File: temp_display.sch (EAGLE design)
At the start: 65 parts, among them IC2 ATMEGA168PROUND, Q1 2N2907

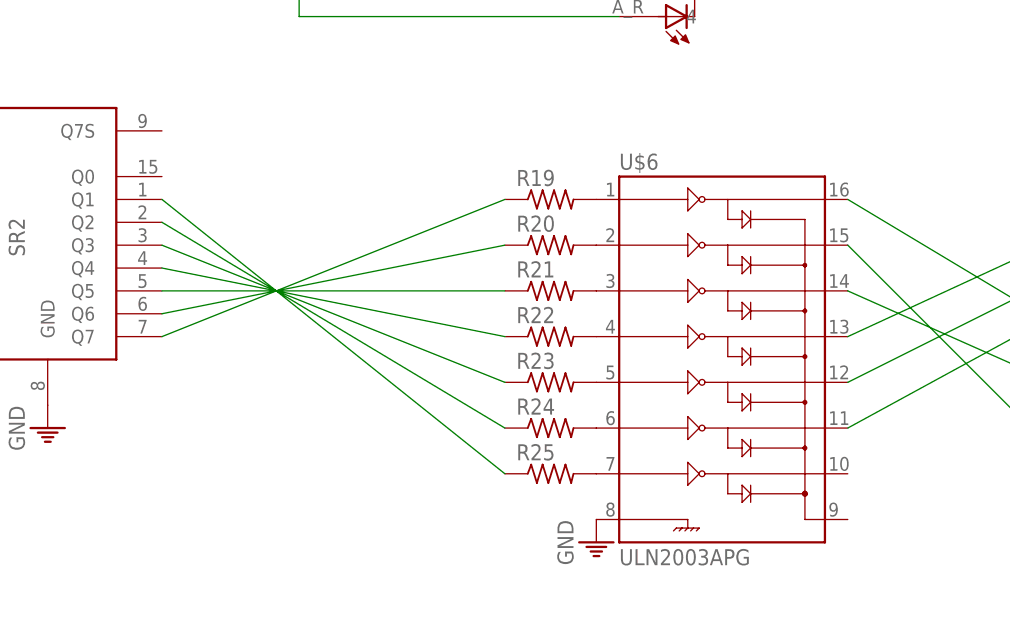
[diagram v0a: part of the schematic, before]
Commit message: Removed resistors from ULN2003 darlington array
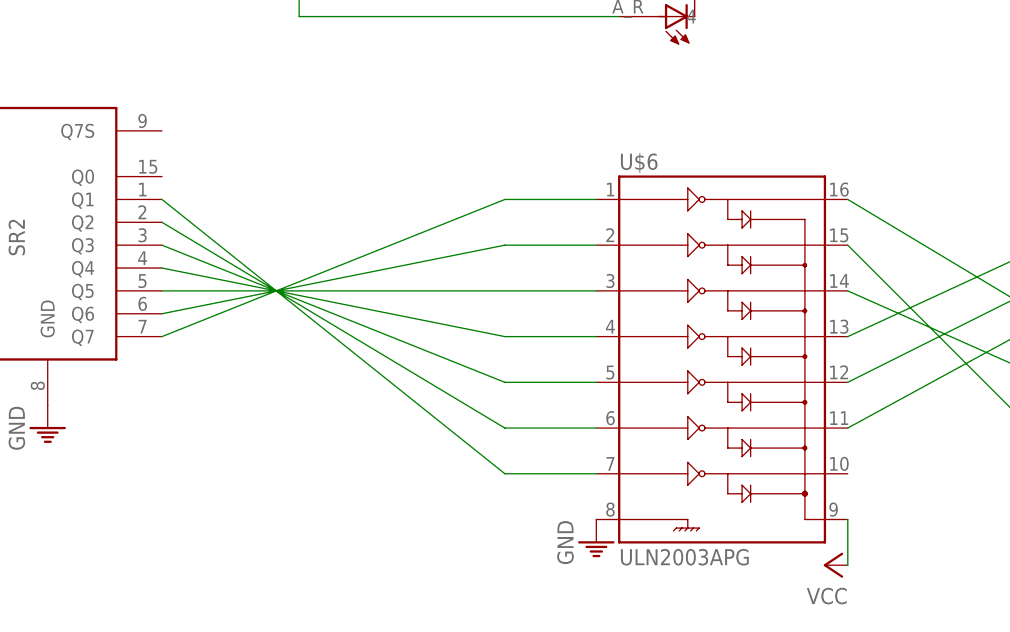
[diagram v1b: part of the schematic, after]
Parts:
- removed R19, R20, R21, R22, R23, R24, R25: (no value), resistor:R-US_0204/7
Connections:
- net N$10 renamed K_L7S_2
- net N$11 renamed K_L7S_1
- net N$13 renamed K_IL34
- net N$14 renamed K_IL12
- net N$59 renamed K_IL56
- net N$60 renamed STCP2
- net N$9 renamed K_L7S_3
- removed net N$16: R19.2, U$6.1
- removed net N$28: R20.2, U$6.2
- removed net N$29: R21.2, U$6.3
- removed net N$32: R22.2, U$6.4
- removed net N$45: R23.2, U$6.5
- removed net N$47: R24.2, U$6.6
- removed net N$49: R25.2, U$6.7
- net N$50: now also U$6.7; no longer R25.1
- net N$53: now also U$6.6; no longer R24.1
- net N$54: now also U$6.5; no longer R23.1
- net N$55: now also U$6.4; no longer R22.1
- net N$56: now also U$6.3; no longer R21.1
- net N$57: now also U$6.2; no longer R20.1
- net N$58: now also U$6.1; no longer R19.1
- net VCC: now also U$6.9

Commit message: Connected 595 shift registers serially.
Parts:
- removed R10, R7, R8, R9: R-USR_POWER-15X8.5, kirill:R-USR_POWER-15X8.5
- removed R15, R16, R17, R18: (no value), resistor:R-US_0204/7
- added R20, R21, R22, R23, R24, R25, R26, R27: 147, resistor:R-US_0204/7
- added R32: (no value), resistor:R-US_0204/7
- added T1: BC547, transistor:BC547
- R1, R2, R3, R4: value (none) -> R-USR_POWER-15X8.5; device resistor:R-US_0204/7 -> kirill:R-USR_POWER-15X8.5
- renumbered R13 to R31, R14 to R30
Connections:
- net N$20 renamed SERIAL_RX
- net N$46 renamed SERIAL_TX
- new net BTH_PW_TRANS: IC2.(PCI0/ICP/CLKO)PB0, R32.1
- new net N$1: SR1.Q7S, SR2.DS
- new net N$2: R32.2, T1.B
- new net N$3: T1.C, U$1.GND, U$1.GND1
- net DS: no longer SR2.DS
- net GND: now also R1.2, R2.2, R3.2, R4.2, T1.E; no longer R10.2, R7.2, R8.2, R9.2, U$1.GND, U$1.GND1
- net N$15: now also R20.1; no longer R1.1
- net N$18: now also R26.1; no longer R17.1
- net N$22: now also R25.1; no longer R15.1
- net N$23: now also R1.1; no longer R5.1
- net N$24: now also R2.1; no longer R6.1
- net N$25: now also R24.1; no longer R16.1
- net N$26: now also R23.1; no longer R4.1
- net N$35: now also R3.1; no longer R7.1
- net N$36: now also R4.1; no longer R8.1
- net N$37: now also R5.1; no longer R9.1
- net N$38: now also R6.1; no longer R10.1
- net N$40: now also R27.1; no longer R18.1
- net N$42: now also R21.1; no longer R2.1
- net N$44: now also R22.1; no longer R3.1
- net SEG_A: now also R27.2; no longer R18.2
- net SEG_B: now also R26.2; no longer R17.2
- net SEG_C: now also R25.2; no longer R15.2
- net SEG_D: now also R24.2; no longer R16.2
- net SEG_DP: now also R20.2; no longer R1.2
- net SEG_E: now also R23.2; no longer R4.2
- net SEG_F: now also R22.2; no longer R3.2
- net SEG_G: now also R21.2; no longer R2.2
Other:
- moved on the sheet: R1, R2, R3, R4, R5, R6

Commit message: Intermediate version: working on the indicator LEDs
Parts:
- removed IL1, IL2, IL3, IL4, IL5, IL6: LED_RGB_CC, kirill:LED_RGB_CC
- added LI1, LI2, LI3, LI4, LI5, LI6: LED_RGB_CC, kirill:LED_RGB_CC
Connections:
- removed net N$33: IC2.(PCI2/SS/OC1B)PB2, S1.1, S1.2
- net K_IL12: now also LI1.K, LI2.K; no longer IL1.3, IL2.3
- net K_IL34: now also LI3.K, LI4.K; no longer IL3.3, IL4.3
- net K_IL56: now also LI5.K, LI6.K; no longer IL5.3, IL6.3
- net N$27: now also S1.1, S1.2
- net SEG_A: now also LI2.R, LI4.R, LI6.R; no longer IL2.1, IL4.1, IL6.1
- net SEG_B: now also LI2.G, LI4.G, LI6.G; no longer IL2.2, IL4.2, IL6.2
- net SEG_C: now also LI2.B, LI4.B, LI6.B; no longer IL2.4, IL4.4, IL6.4
- net SEG_D: now also LI1.R, LI3.R, LI5.R; no longer IL1.1, IL3.1, IL5.1
- net SEG_E: now also LI1.G, LI3.G, LI5.G; no longer IL1.2, IL3.2, IL5.2
- net SEG_F: now also LI1.B, LI3.B, LI5.B; no longer IL1.4, IL3.4, IL5.4

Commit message: 
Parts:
- added D1: 1N4004, adafruit:1N4004
- added R7: (no value), resistor:R-US_0204/7
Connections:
- removed net N$39: C3.1, IC1.IN, POWER_SW.2
- new net +3V3: C4.1, D1.C, IC1.OUT, IC1.OUT@1, U$1.VCC
- new net +5V: C1.+, C2.2, C3.1, IC1.IN, IC2.AVCC, IC2.VCC, JP8.4, JP9.11, JP9.15, JP9.19, JP9.23, JP9.3, JP9.7, POWER_SW.2, Q1.E, SR1.MR, SR1.VCC, SR2.MR, SR2.VCC, U$6.9
- new net N$4: D1.A, R7.2, U$1.UART_RX
- net SERIAL_RX: now also R7.1; no longer U$1.UART_RX
- net VCC: no longer C1.+, C2.2, C4.1, IC1.OUT, IC1.OUT@1, IC2.AVCC, IC2.VCC, JP8.4, JP9.11, JP9.15, JP9.19, JP9.23, JP9.3, JP9.7, Q1.E, SR1.MR, SR1.VCC, SR2.MR, SR2.VCC, U$1.VCC, U$6.9
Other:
- moved on the sheet: BAT1, BAT2, C3, C4, IC1, POWER_SW

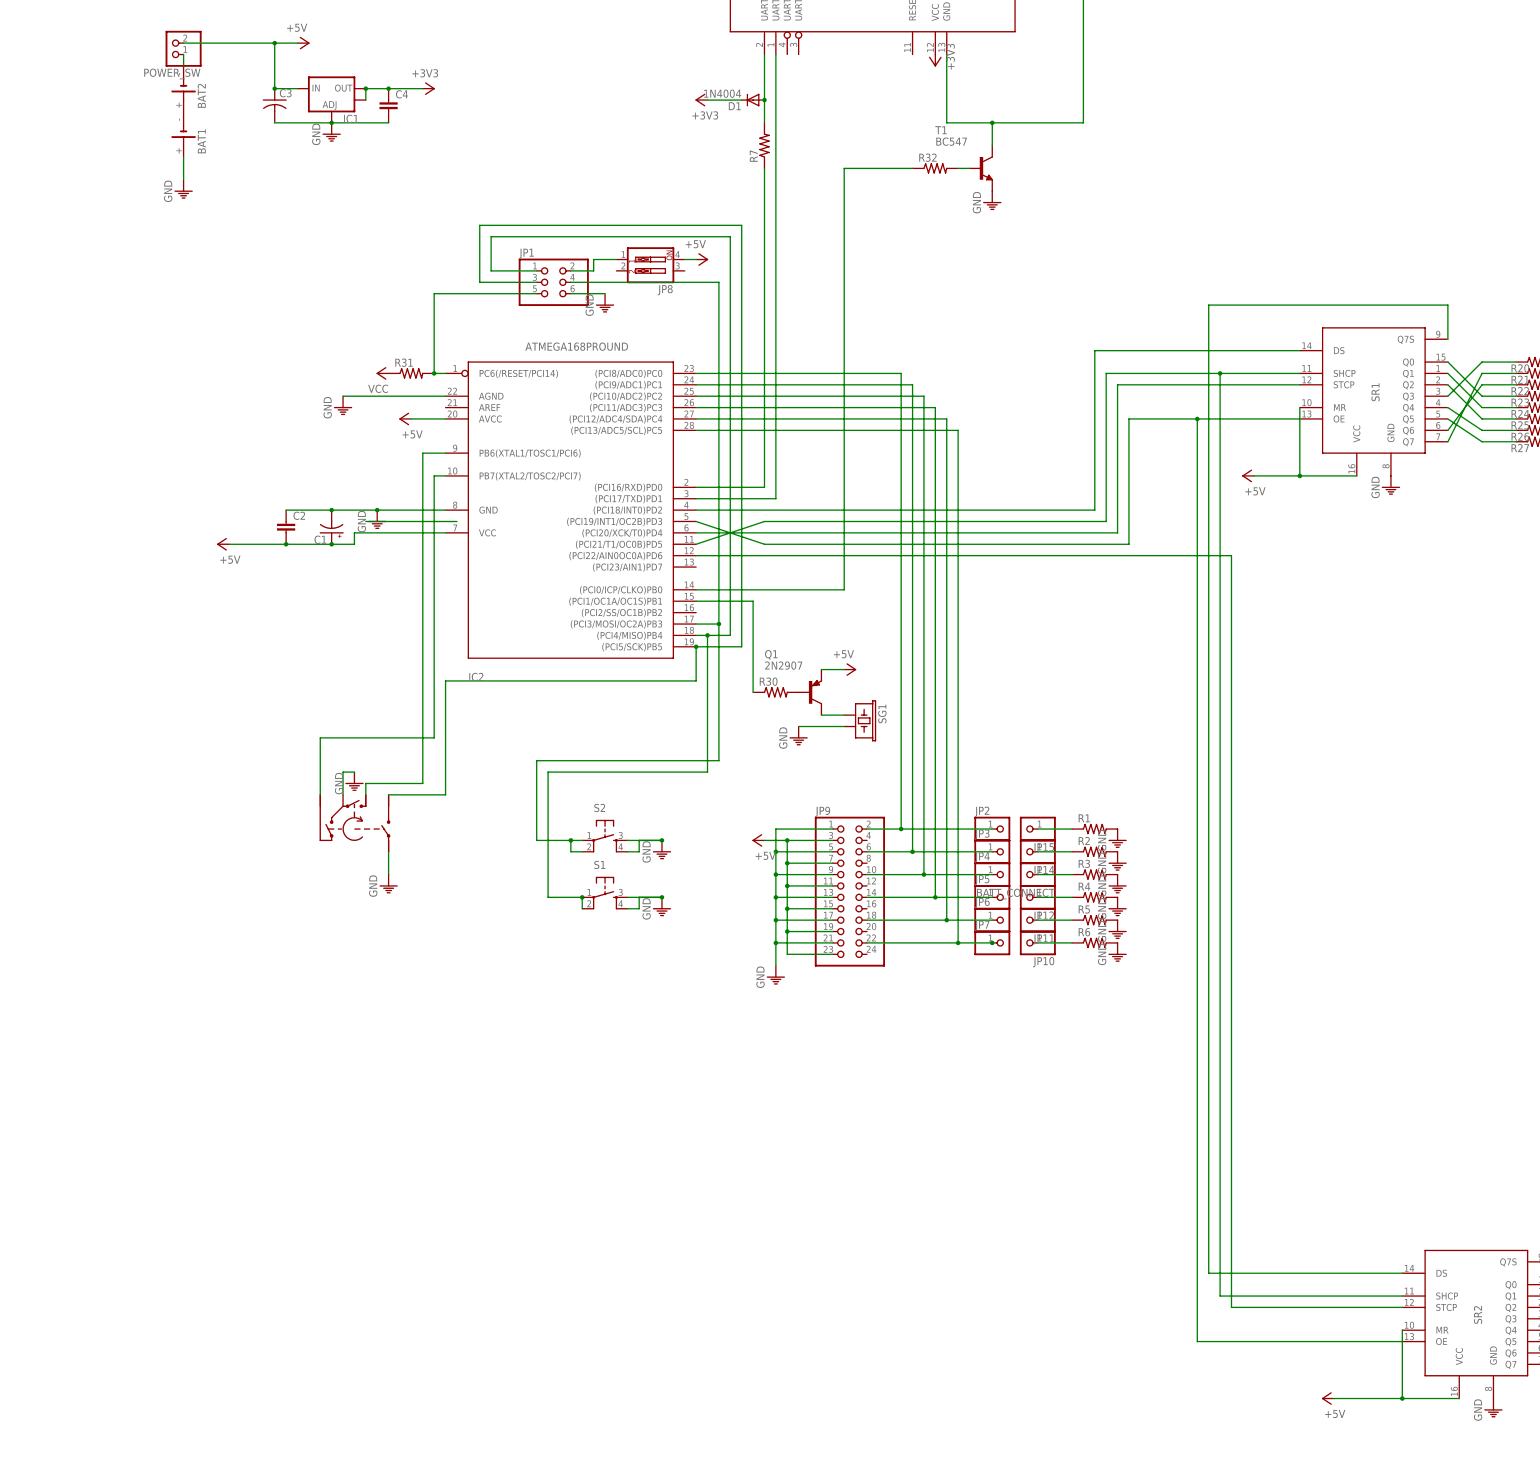
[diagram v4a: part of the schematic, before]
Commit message: Last version with CR2032 batteries
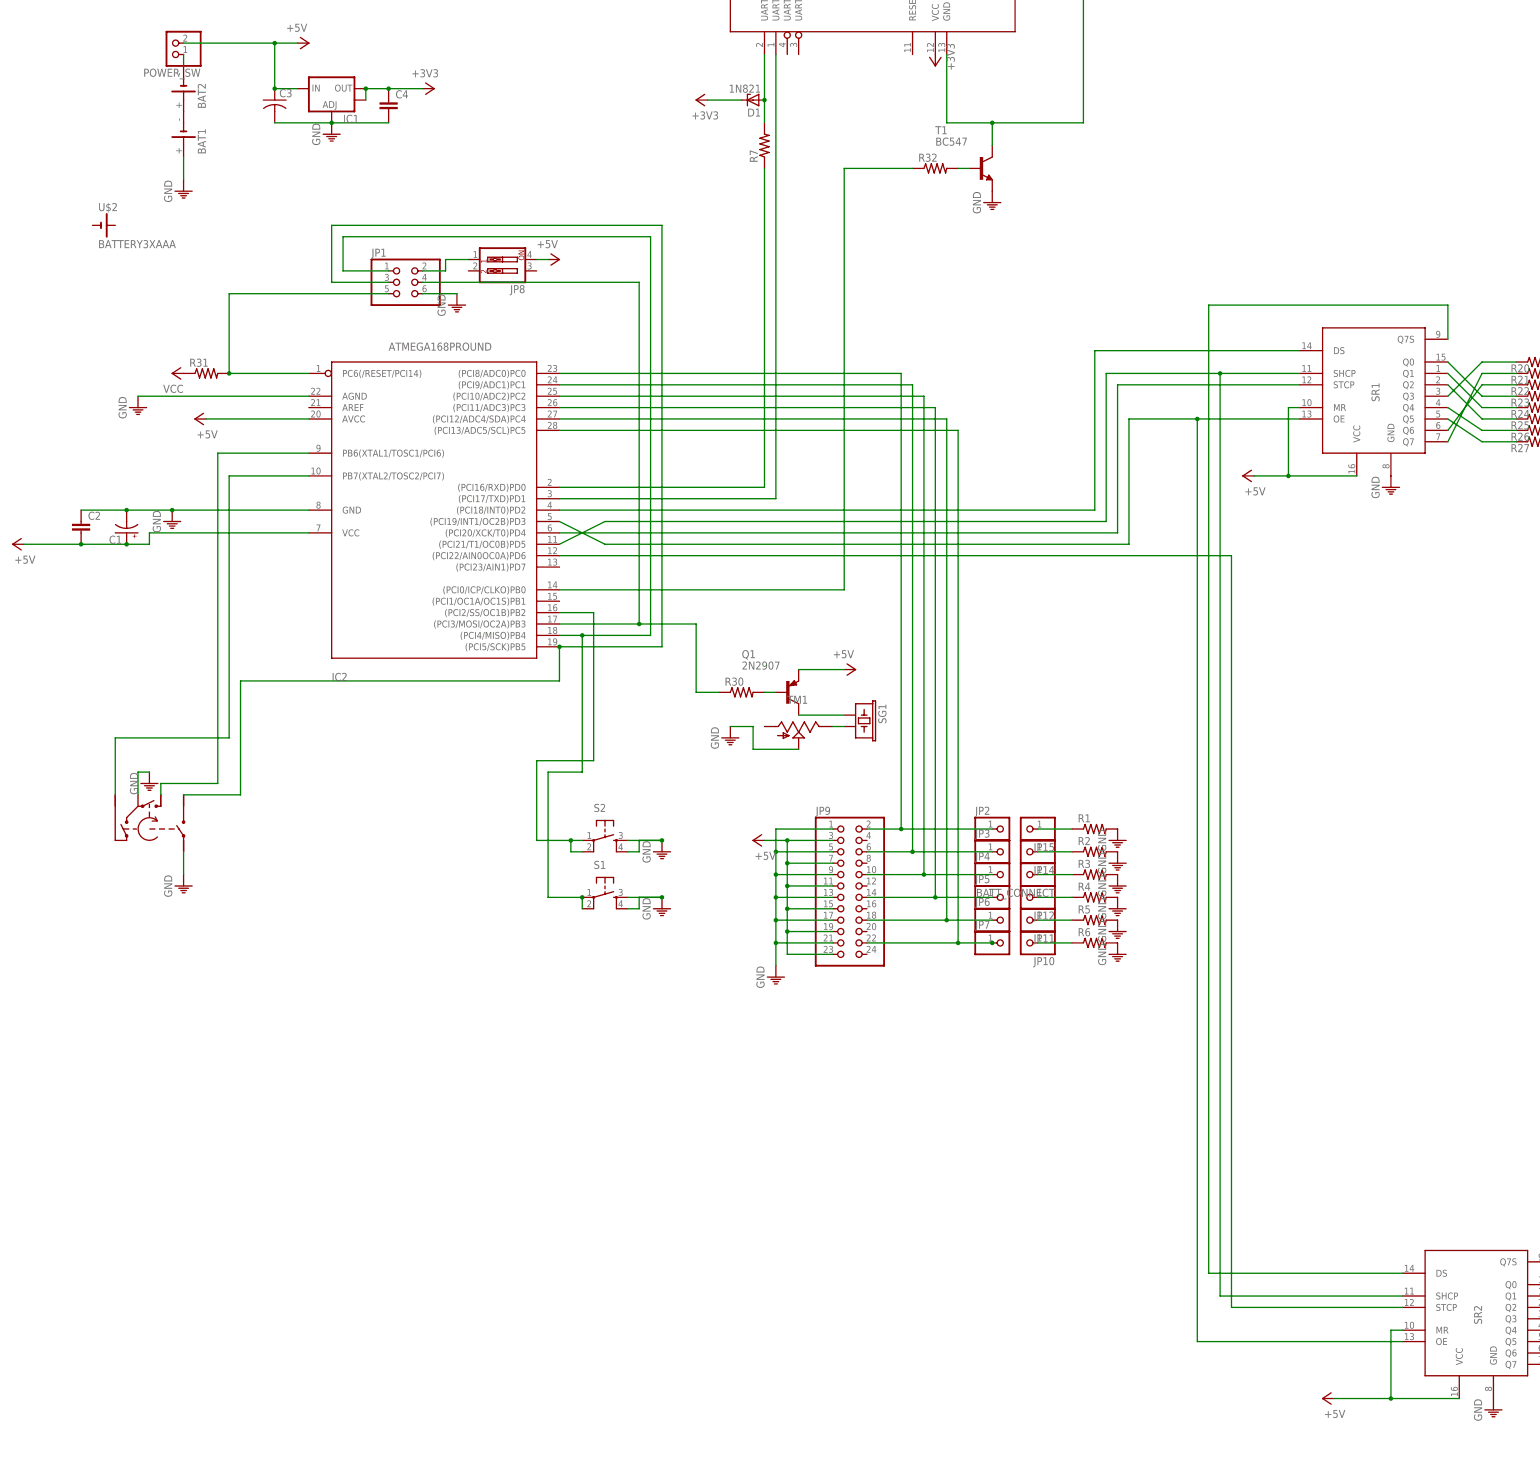
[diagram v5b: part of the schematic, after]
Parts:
- added TM1: TRIMPOT, kirill:TRIMPOT
- added U$2: BATTERY3XAAA, kirill:BATTERY3XAAA
- D1: value 1N4004 -> 1N821; device adafruit:1N4004 -> diode:1N821
- JP1: device pinhead:PINHD-2X3/90 -> pinhead:PINHD-2X3
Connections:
- removed net N$48: IC2.(PCI1/OC1A/OC1S)PB1, R30.1
- new net N$5: IC2.(PCI2/SS/OC1B)PB2, S2.1, S2.2
- new net N$6: SG1.2, TM1.E
- net GND: now also TM1.S; no longer SG1.2
- net N$34: now also R30.1; no longer S2.1, S2.2
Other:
- moved on the sheet: C1, C2, IC2, JP1, JP8, Q1, R30, R31

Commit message: 
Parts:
- removed BAT1, BAT2: BATTERY_CR2032, kirill:BATTERY_CR2032
- added LI7: LED_RGB_CC, kirill:LED_RGB_CC
- JP8: device SparkFun:SW_DIP-2 -> pinhead:PINHD-1X2
- R30: device resistor:R-US_0204/7 -> resistor:R-US_0207/10
- R31: device resistor:R-US_0204/7 -> resistor:R-US_0204/5
- R7: value (none) -> 1K
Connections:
- net K_IL56 renamed K_IL567
- net N$43 renamed MROUTE
- net N$50 renamed CAT_1
- net N$53 renamed CAT_2
- net N$54 renamed CAT_3
- net N$55 renamed CAT_4
- net N$56 renamed CAT_5
- net N$57 renamed CAT_6
- net N$58 renamed CAT_7
- removed net B1: BAT2.-, POWER_SW.1
- removed net BATT_CONNECT: BAT1.-, BAT2.+
- removed net N$30: JP1.2, JP8.1
- removed net VCC: R31.1
- new net +5: C1.+, C2.2, C3.1, IC1.IN, IC2.AVCC, IC2.VCC, JP1.2, JP9.11, JP9.15, JP9.19, JP9.23, JP9.3, JP9.7, POWER_SW.2, Q1.E, R31.1, SR1.MR, SR1.VCC, SR2.MR, SR2.VCC, U$6.9
- new net N$7: LI7.K, U$6.10
- new net N$9: SR2.Q0
- net +5V: now also JP8.1, POWER_SW.1; no longer C1.+, C2.2, C3.1, IC1.IN, IC2.AVCC, IC2.VCC, JP8.4, JP9.11, JP9.15, JP9.19, JP9.23, JP9.3, JP9.7, POWER_SW.2, Q1.E, SR1.MR, SR1.VCC, SR2.MR, SR2.VCC, U$6.9
- net GND: now also JP8.2; no longer BAT1.+, U$1.GND2
- net N$3: no longer U$1.GND1
- net N$6: now also TM1.A; no longer TM1.E
- net SEG_A: now also LI7.R
- net SEG_B: now also LI7.G
- net SEG_C: now also LI7.B
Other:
- moved on the sheet: LI1, LI2, LI3, LI4, LI5, LI6, SR2, TM1, U$2, U$6
